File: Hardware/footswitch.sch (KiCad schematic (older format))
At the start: 18 parts, among them J9 FootSW, U1 74HC14, U4 EL817, U5 EL817

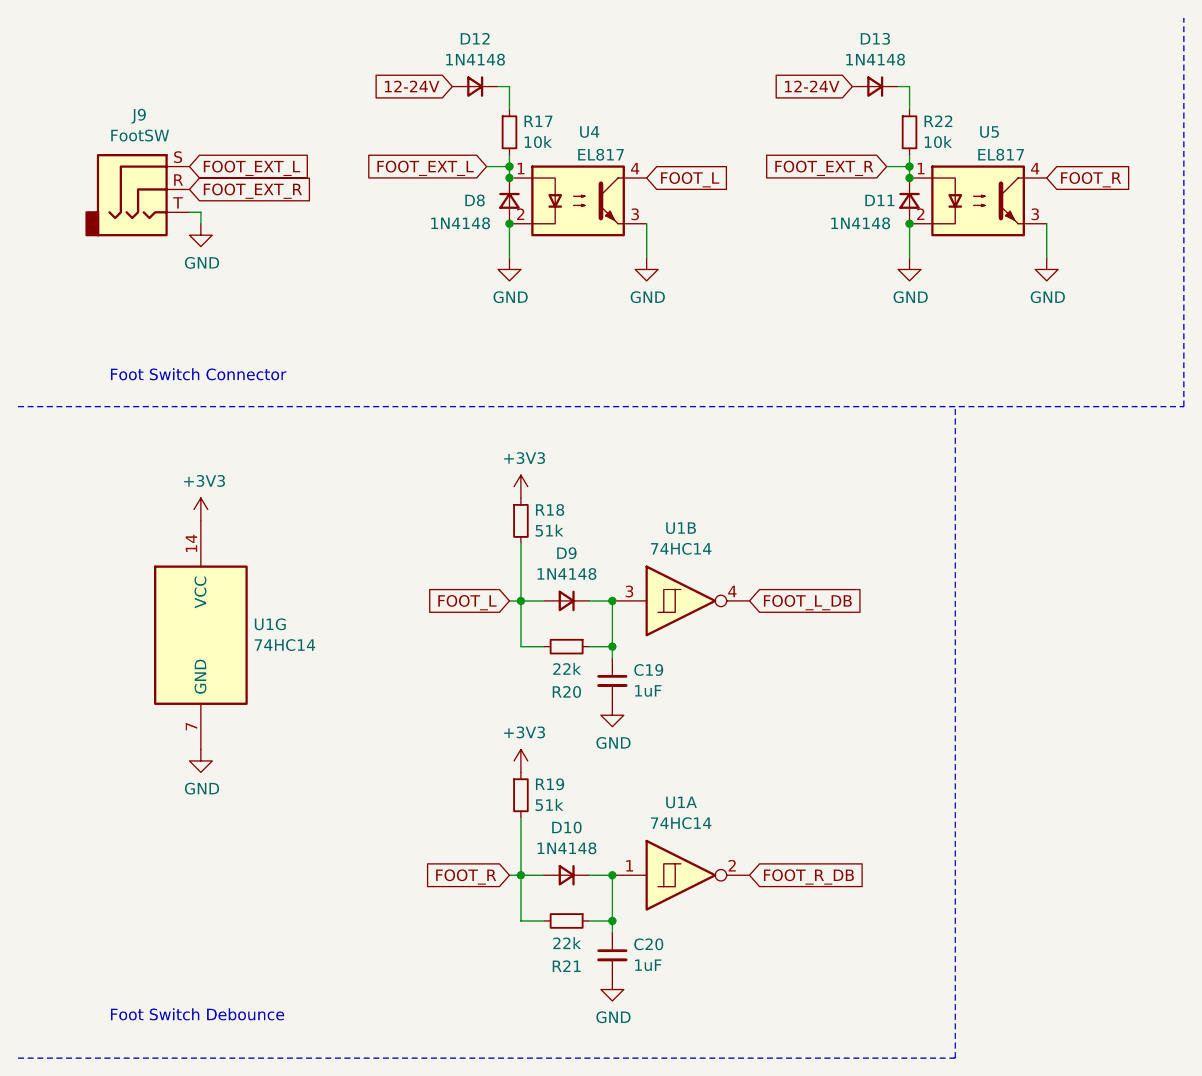
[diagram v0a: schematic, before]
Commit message: Board updates:
Fixed footprints (SMD vs. THT, no hanging pads in the air)
Added mounting holes for production
Moved F.Fab text to readable locations
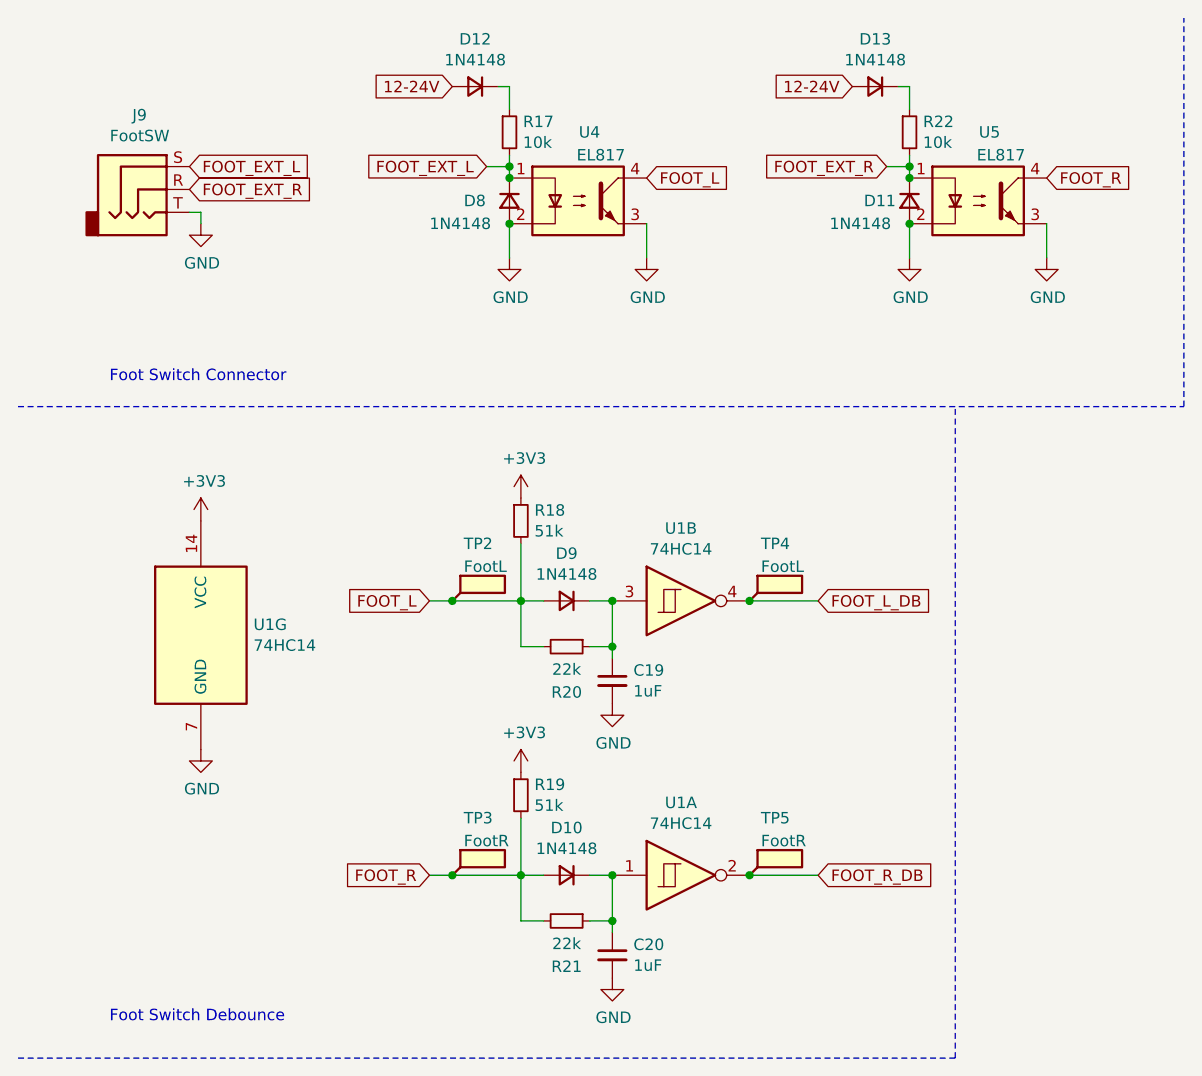
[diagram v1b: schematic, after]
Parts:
- added TP2, TP4: FootL, Measurement_Points:Measurement_Point_Round-SMD-Pad_Small, symbol Connector:TestPoint_Flag
- added TP3, TP5: FootR, Measurement_Points:Measurement_Point_Round-SMD-Pad_Small, symbol Connector:TestPoint_Flag
- U4, U5: footprint Housings_DIP:DIP-4_W7.62mm_LongPads -> Housings_SOIC:SO-4_7.6x3.6mm_Pitch2.54mm
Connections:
- net FOOT_L: now also TP2.1
- net FOOT_L_DB: now also TP4.1
- net FOOT_R: now also TP3.1
- net FOOT_R_DB: now also TP5.1
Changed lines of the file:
@@
 	1    0    0    -1
 $EndComp
-Text GLabel 3700 3050 2    50   Input ~ 0
+Text GLabel 4000 3050 2    50   Input ~ 0
 FOOT_L_DB
-Text GLabel 2650 3050 0    50   Input ~ 0
+Text GLabel 2300 3050 0    50   Input ~ 0
 FOOT_L
 $Comp
@@
 Connection ~ 2700 3050
 Wire Wire Line
-	2700 3050 2650 3050
-Wire Wire Line
 	3100 3050 3000 3050
 Connection ~ 3100 3050
@@
 	1    0    0    -1
 $EndComp
-Text GLabel 2650 4250 0    50   Input ~ 0
+Text GLabel 2300 4250 0    50   Input ~ 0
 FOOT_R
 $Comp
@@
 Connection ~ 2700 4250
 Wire Wire Line
-	2700 4250 2650 4250
-Wire Wire Line
 	3100 4250 3000 4250
 Wire Wire Line
@@
 $EndComp
 Connection ~ 3100 4250
-Text GLabel 3700 4250 2    50   Input ~ 0
+Text GLabel 4000 4250 2    50   Input ~ 0
 FOOT_R_DB
 Text Notes 900  4900 0    50   ~ 0
@@
 F 0 "U4" H 3000 1600 50  0000 C CNN
 F 1 "EL817" H 3050 1500 50  0000 C CNN
-F 2 "Housings_DIP:DIP-4_W7.62mm_LongPads" H 2750 1100 50  0001 L CIN
+F 2 "Housings_SOIC:SO-4_7.6x3.6mm_Pitch2.54mm" H 2750 1100 50  0001 L CIN
 F 3 "http://www.everlight.com/file/ProductFile/EL817.pdf" H 2950 1300 50  0001 L CNN
 F 4 "C106900" H 2950 1300 50  0001 C CNN "LCSC"
@@
 F 0 "U5" H 4750 1600 50  0000 C CNN
 F 1 "EL817" H 4800 1500 50  0000 C CNN
-F 2 "Housings_DIP:DIP-4_W7.62mm_LongPads" H 4500 1100 50  0001 L CIN
+F 2 "Housings_SOIC:SO-4_7.6x3.6mm_Pitch2.54mm" H 4500 1100 50  0001 L CIN
 F 3 "http://www.everlight.com/file/ProductFile/EL817.pdf" H 4700 1300 50  0001 L CNN
 F 4 "C106900" H 4700 1300 50  0001 C CNN "LCSC"
@@
 	-1   0    0    1
 $EndComp
+$Comp
+L Connector:TestPoint_Flag TP4
+U 1 1 5FA27E9E
+P 3700 3050
+F 0 "TP4" H 3750 3300 50  0000 L CNN
+F 1 "FootL" H 3750 3200 50  0000 L CNN
+F 2 "Measurement_Points:Measurement_Point_Round-SMD-Pad_Small" H 3900 3050 50  0001 C CNN
+F 3 "~" H 3900 3050 50  0001 C CNN
+	1    3700 3050
+	1    0    0    -1
+$EndComp
+Connection ~ 3700 3050
+Wire Wire Line
+	3700 3050 4000 3050
+$Comp
+L Connector:TestPoint_Flag TP5
+U 1 1 5FA290A1
+P 3700 4250
+F 0 "TP5" H 3750 4500 50  0000 L CNN
+F 1 "FootR" H 3750 4400 50  0000 L CNN
+F 2 "Measurement_Points:Measurement_Point_Round-SMD-Pad_Small" H 3900 4250 50  0001 C CNN
+F 3 "~" H 3900 4250 50  0001 C CNN
+	1    3700 4250
+	1    0    0    -1
+$EndComp
+Connection ~ 3700 4250
+Wire Wire Line
+	3700 4250 4000 4250
+Wire Wire Line
+	2300 3050 2400 3050
+$Comp
+L Connector:TestPoint_Flag TP2
+U 1 1 5FA2A61B
+P 2400 3050
+F 0 "TP2" H 2450 3300 50  0000 L CNN
+F 1 "FootL" H 2450 3200 50  0000 L CNN
+F 2 "Measurement_Points:Measurement_Point_Round-SMD-Pad_Small" H 2600 3050 50  0001 C CNN
+F 3 "~" H 2600 3050 50  0001 C CNN
+	1    2400 3050
+	1    0    0    -1
+$EndComp
+Connection ~ 2400 3050
+Wire Wire Line
+	2400 3050 2700 3050
+Wire Wire Line
+	2300 4250 2400 4250
+$Comp
+L Connector:TestPoint_Flag TP3
+U 1 1 5FA2B2F1
+P 2400 4250
+F 0 "TP3" H 2450 4500 50  0000 L CNN
+F 1 "FootR" H 2450 4400 50  0000 L CNN
+F 2 "Measurement_Points:Measurement_Point_Round-SMD-Pad_Small" H 2600 4250 50  0001 C CNN
+F 3 "~" H 2600 4250 50  0001 C CNN
+	1    2400 4250
+	1    0    0    -1
+$EndComp
+Connection ~ 2400 4250
+Wire Wire Line
+	2400 4250 2700 4250
 $EndSCHEMATC

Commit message: Hardware v0.1, Firmware runs ADC trigger by TIM3
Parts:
- U1: LCSC (none) -> C5605
- U4, U5: footprint Housings_SOIC:SO-4_7.6x3.6mm_Pitch2.54mm -> Hardware:SO-4_7.6x3.6mm_Pitch2.54mm
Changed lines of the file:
@@
 F 2 "Housings_SOIC:SOIC-14_3.9x8.7mm_Pitch1.27mm" H 3400 4250 50  0001 C CNN
 F 3 "http://www.ti.com/lit/gpn/sn74HC14" H 3400 4250 50  0001 C CNN
+F 4 "C5605" H 3400 4250 50  0001 C CNN "LCSC"
 	1    3400 4250
 	1    0    0    -1
@@
 F 2 "Housings_SOIC:SOIC-14_3.9x8.7mm_Pitch1.27mm" H 3400 3050 50  0001 C CNN
 F 3 "http://www.ti.com/lit/gpn/sn74HC14" H 3400 3050 50  0001 C CNN
+F 4 "C5605" H 3400 3050 50  0001 C CNN "LCSC"
 	2    3400 3050
 	1    0    0    -1
@@
 F 0 "U4" H 3000 1600 50  0000 C CNN
 F 1 "EL817" H 3050 1500 50  0000 C CNN
-F 2 "Housings_SOIC:SO-4_7.6x3.6mm_Pitch2.54mm" H 2750 1100 50  0001 L CIN
+F 2 "Hardware:SO-4_7.6x3.6mm_Pitch2.54mm" H 2750 1100 50  0001 L CIN
 F 3 "http://www.everlight.com/file/ProductFile/EL817.pdf" H 2950 1300 50  0001 L CNN
 F 4 "C106900" H 2950 1300 50  0001 C CNN "LCSC"
@@
 F 0 "U5" H 4750 1600 50  0000 C CNN
 F 1 "EL817" H 4800 1500 50  0000 C CNN
-F 2 "Housings_SOIC:SO-4_7.6x3.6mm_Pitch2.54mm" H 4500 1100 50  0001 L CIN
+F 2 "Hardware:SO-4_7.6x3.6mm_Pitch2.54mm" H 4500 1100 50  0001 L CIN
 F 3 "http://www.everlight.com/file/ProductFile/EL817.pdf" H 4700 1300 50  0001 L CNN
 F 4 "C106900" H 4700 1300 50  0001 C CNN "LCSC"
